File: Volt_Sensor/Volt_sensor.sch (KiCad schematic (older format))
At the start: 23 parts, among them P1 CONN_01X03, P2 CONN_01X02, P3 CONN_01X02, P4 CONN_01X02, U1 LV-25-P, U2 NE5532

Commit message: Changed pot meter
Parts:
- removed RV1: 100k, potentiometer:Potentiometer_Trimmer-Suntan-TSR-3386P, symbol POT-RESCUE-Volt_sensor
- added RV1: 100k, symbol POT
- RV2: symbol POT-RESCUE-Volt_sensor -> POT
- U1: footprint LEM:LV25-P -> Hall-Effect_Transducers_LEM:LV25-P
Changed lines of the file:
@@
 F 0 "U1" H 5800 2200 60  0000 C CNN
 F 1 "LV-25-P" H 6350 1400 60  0000 C CNN
-F 2 "LEM:LV25-P" H 6100 1800 60  0001 C CNN
+F 2 "Hall-Effect_Transducers_LEM:LV25-P" H 6100 1800 60  0001 C CNN
 F 3 "" H 6100 1800 60  0001 C CNN
 	1    6150 1800
@@
 $EndComp
 $Comp
-L POT-RESCUE-Volt_sensor RV1
-U 1 1 583ED8DC
-P 8750 1600
-F 0 "RV1" H 8750 1520 50  0000 C CNN
-F 1 "100k" H 8750 1600 50  0000 C CNN
-F 2 "potentiometer:Potentiometer_Trimmer-Suntan-TSR-3386P" H 8750 1600 50  0001 C CNN
-F 3 "" H 8750 1600 50  0000 C CNN
-	1    8750 1600
-	0    1    1    0
-$EndComp
-$Comp
 L VCC #PWR010
 U 1 1 583ED9DE
@@
 Measurement/\nbypass point
 $Comp
-L POT-RESCUE-Volt_sensor RV2
+L POT RV2
 U 1 1 58501A90
 P 9950 2300
-F 0 "RV2" H 9950 2220 50  0000 C CNN
-F 1 "50k" H 9950 2300 50  0000 C CNN
+F 0 "RV2" V 9850 2300 50  0000 C CNN
+F 1 "50k" V 9950 2300 50  0000 C CNN
 F 2 "potentiometer:Potentiometer_Trimmer-Suntan-TSR-3386P" H 9950 2300 50  0001 C CNN
 F 3 "" H 9950 2300 50  0000 C CNN
 	1    9950 2300
-	-1   0    0    1
+	0    1    1    0
 $EndComp
 Text Notes 9850 2800 0    60   ~ 0
@@
 Text Notes 1200 1850 0    60   ~ 0
 + 15V DC
+$Comp
+L POT RV1
+U 1 1 5980BD14
+P 8750 1600
+F 0 "RV1" V 8650 1600 50  0000 C CNN
+F 1 "100k" V 8750 1600 50  0000 C CNN
+F 2 "" H 8750 1600 50  0001 C CNN
+F 3 "" H 8750 1600 50  0001 C CNN
+	1    8750 1600
+	1    0    0    -1
+$EndComp
 $EndSCHEMATC

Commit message: Updated current sensor card
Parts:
- RV1: footprint (none) -> Potentiometers:Potentiometer_Trimmer_ACP_CA6v_Horizontal
- RV2: footprint potentiometer:Potentiometer_Trimmer-Suntan-TSR-3386P -> Potentiometers:Potentiometer_Trimmer_ACP_CA6v_Horizontal
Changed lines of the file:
@@
 F 0 "RV2" V 9850 2300 50  0000 C CNN
 F 1 "50k" V 9950 2300 50  0000 C CNN
-F 2 "potentiometer:Potentiometer_Trimmer-Suntan-TSR-3386P" H 9950 2300 50  0001 C CNN
+F 2 "Potentiometers:Potentiometer_Trimmer_ACP_CA6v_Horizontal" H 9950 2300 50  0001 C CNN
 F 3 "" H 9950 2300 50  0000 C CNN
 	1    9950 2300
@@
 F 0 "RV1" V 8650 1600 50  0000 C CNN
 F 1 "100k" V 8750 1600 50  0000 C CNN
-F 2 "" H 8750 1600 50  0001 C CNN
+F 2 "Potentiometers:Potentiometer_Trimmer_ACP_CA6v_Horizontal" H 8750 1600 50  0001 C CNN
 F 3 "" H 8750 1600 50  0001 C CNN
 	1    8750 1600

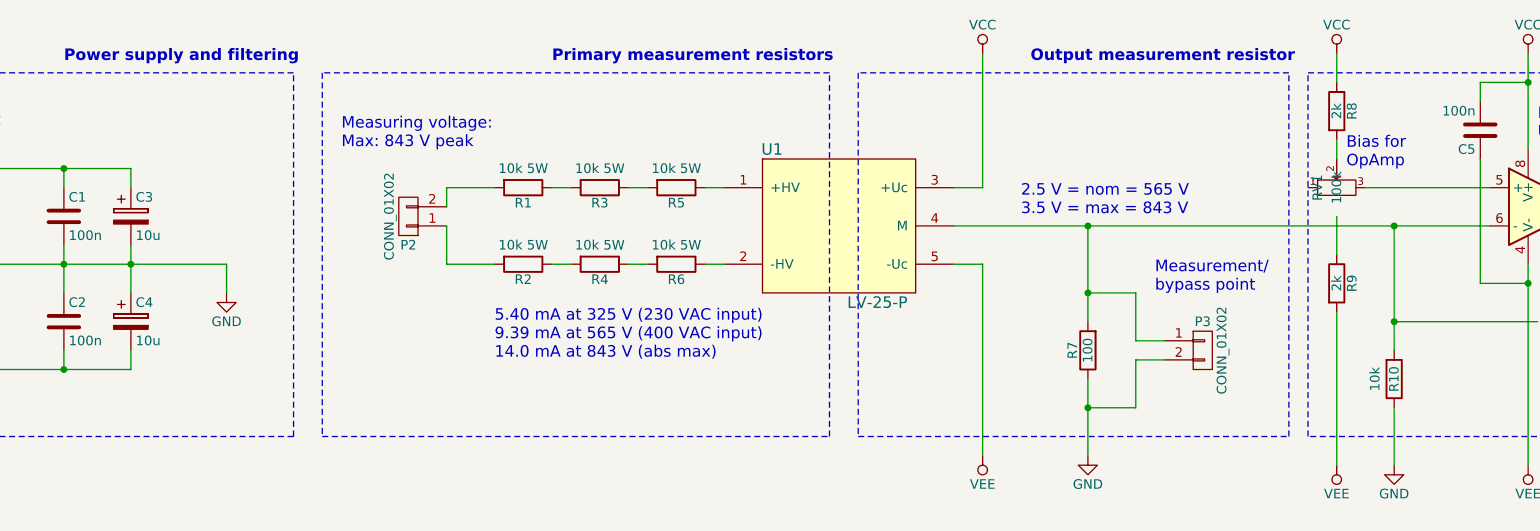
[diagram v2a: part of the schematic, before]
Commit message: Updated component values and highlighted errors and/or improvement possibilities for next revision
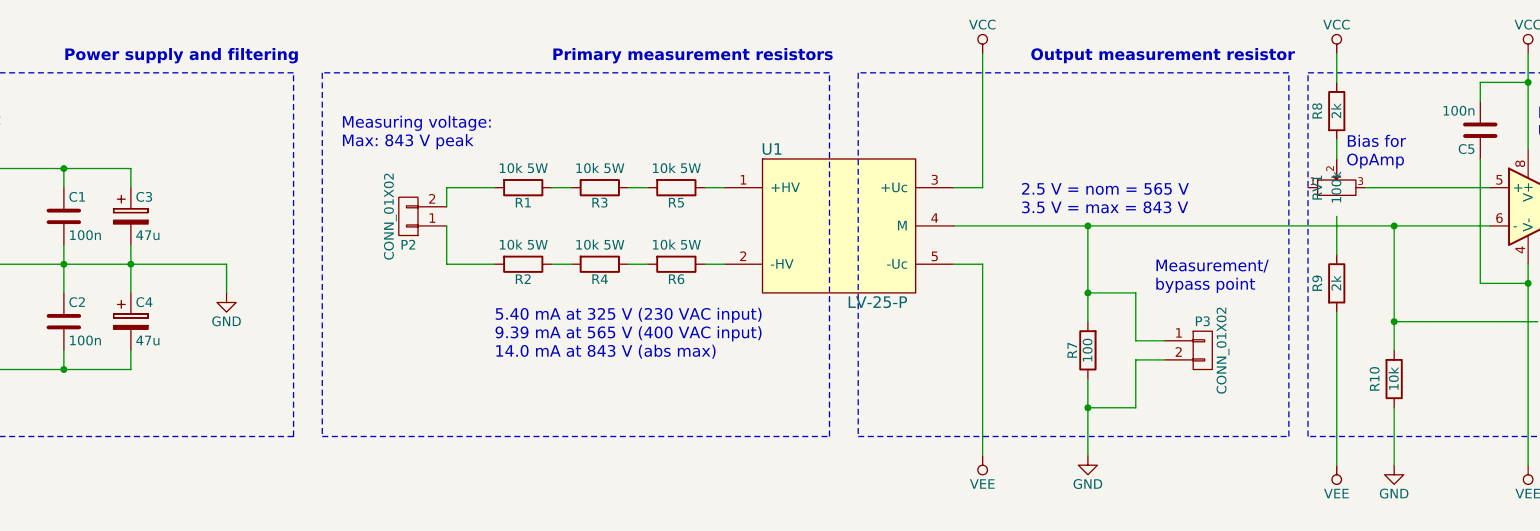
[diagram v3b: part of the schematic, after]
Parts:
- C3, C4: value 10u -> 47u
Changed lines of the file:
@@
 P 2450 2300
 F 0 "C4" H 2475 2400 50  0000 L CNN
-F 1 "10u" H 2475 2200 50  0000 L CNN
+F 1 "47u" H 2475 2200 50  0000 L CNN
 F 2 "Capacitors_THT:C_Radial_D5_L11_P2.5" H 2488 2150 50  0001 C CNN
 F 3 "" H 2450 2300 50  0000 C CNN
@@
 P 2450 1750
 F 0 "C3" H 2475 1850 50  0000 L CNN
-F 1 "10u" H 2475 1650 50  0000 L CNN
+F 1 "47u" H 2475 1650 50  0000 L CNN
 F 2 "Capacitors_THT:C_Radial_D5_L11_P2.5" H 2488 1600 50  0001 C CNN
 F 3 "" H 2450 1750 50  0000 C CNN
@@
 U 1 1 583ED80A
 P 8750 1200
-F 0 "R8" V 8830 1200 50  0000 C CNN
+F 0 "R8" V 8650 1200 50  0000 C CNN
 F 1 "2k" V 8750 1200 50  0000 C CNN
 F 2 "Resistors_SMD:R_1206_HandSoldering" V 8680 1200 50  0001 C CNN
@@
 U 1 1 583ED874
 P 8750 2100
-F 0 "R9" V 8830 2100 50  0000 C CNN
+F 0 "R9" V 8650 2100 50  0000 C CNN
 F 1 "2k" V 8750 2100 50  0000 C CNN
 F 2 "Resistors_SMD:R_1206_HandSoldering" V 8680 2100 50  0001 C CNN
@@
 U 1 1 583EE3A2
 P 9050 2600
-F 0 "R10" V 9050 2600 50  0000 C CNN
-F 1 "10k" V 8950 2600 50  0000 C CNN
+F 0 "R10" V 8950 2600 50  0000 C CNN
+F 1 "10k" V 9050 2600 50  0000 C CNN
 F 2 "Resistors_SMD:R_1206_HandSoldering" V 8980 2600 50  0001 C CNN
 F 3 "" H 9050 2600 50  0000 C CNN

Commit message: Removed some hard-coded paths
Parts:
- C1, C2, C5: symbol C -> device:C
- C3, C4: symbol CP -> device:CP
- P1: symbol CONN_01X03 -> conn:Conn_01x03
- P2, P3, P4: symbol CONN_01X02 -> conn:Conn_01x02
- R1, R10, R2, R3, R4, R5, R6, R7, R8, R9: symbol R -> device:R
- RV1, RV2: symbol POT -> device:POT
- U1: symbol LV-25-P -> LEM:LV-25-P
- U2: symbol NE5532 -> linear:NE5532
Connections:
- wire segments 59 -> 76
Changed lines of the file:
@@
-EESchema Schematic File Version 2
-LIBS:power
-LIBS:device
-LIBS:transistors
-LIBS:conn
-LIBS:linear
-LIBS:regul
-LIBS:74xx
-LIBS:cmos4000
-LIBS:adc-dac
-LIBS:memory
-LIBS:xilinx
-LIBS:microcontrollers
-LIBS:dsp
-LIBS:microchip
-LIBS:analog_switches
-LIBS:motorola
-LIBS:texas
-LIBS:intel
-LIBS:audio
-LIBS:interface
-LIBS:digital-audio
-LIBS:philips
-LIBS:display
-LIBS:cypress
-LIBS:siliconi
-LIBS:opto
-LIBS:atmel
-LIBS:contrib
-LIBS:valves
-LIBS:LEM
-LIBS:Volt_sensor-cache
-EELAYER 25 0
+EESchema Schematic File Version 4
+EELAYER 26 0
 EELAYER END
 $Descr A4 11693 8268
@@
 $EndDescr
 $Comp
-L LV-25-P U1
+L LEM:LV-25-P U1
 U 1 1 583EA5FB
 P 6150 1800
@@
 $EndComp
 $Comp
-L R R1
+L device:R R1
 U 1 1 583EABE7
 P 4500 1600
@@
 $EndComp
 $Comp
-L R R5
+L device:R R5
 U 1 1 583EB13D
 P 5300 1600
@@
 $EndComp
 $Comp
-L R R3
+L device:R R3
 U 1 1 583EB1AE
 P 4900 1600
@@
 $EndComp
 $Comp
-L R R2
+L device:R R2
 U 1 1 583EB1DF
 P 4500 2000
@@
 $EndComp
 $Comp
-L R R6
+L device:R R6
 U 1 1 583EB204
 P 5300 2000
@@
 $EndComp
 $Comp
-L R R4
+L device:R R4
 U 1 1 583EB232
 P 4900 2000
@@
 $EndComp
 $Comp
-L VEE #PWR01
+L power:VEE #PWR01
 U 1 1 583EB25D
 P 6900 3000
@@
 $EndComp
 $Comp
-L VCC #PWR02
+L power:VCC #PWR02
 U 1 1 583EB2AE
 P 6900 900
@@
 $EndComp
 $Comp
-L R R7
+L device:R R7
 U 1 1 583EB372
 P 7450 2450
@@
 $EndComp
 $Comp
-L CONN_01X02 P2
+L conn:Conn_01x02 P2
 U 1 1 583EB545
 P 3900 1750
@@
 $EndComp
 $Comp
-L CONN_01X03 P1
+L conn:Conn_01x03 P1
 U 1 1 583EB6EF
 P 1000 2000
@@
 $EndComp
 $Comp
-L VEE #PWR03
+L power:VEE #PWR03
 U 1 1 583EBA34
 P 1700 2650
@@
 $EndComp
 $Comp
-L VCC #PWR04
+L power:VCC #PWR04
 U 1 1 583EBA60
 P 1700 1400
@@
 $EndComp
 $Comp
-L GND #PWR05
+L power:GND #PWR05
 U 1 1 583EBA8E
 P 7450 3000
@@
 $EndComp
 $Comp
-L GND #PWR06
+L power:GND #PWR06
 U 1 1 583EBAC1
 P 2950 2150
@@
 $EndComp
 $Comp
-L CP C4
+L device:CP C4
 U 1 1 583EBB43
 P 2450 2300
@@
 $EndComp
 $Comp
-L CP C3
+L device:CP C3
 U 1 1 583EBBE1
 P 2450 1750
@@
 $EndComp
 $Comp
-L C C1
+L device:C C1
 U 1 1 583EC499
 P 2100 1750
@@
 $EndComp
 $Comp
-L C C2
+L device:C C2
 U 1 1 583EC55E
 P 2100 2300
@@
 Measuring voltage:\nMax: 843 V peak
 $Comp
-L CONN_01X02 P3
+L conn:Conn_01x02 P3
 U 1 1 583EC98A
 P 8050 2450
@@
 2.5 V = nom = 565 V\n3.5 V = max = 843 V
 $Comp
-L NE5532 U2
+L linear:NE5532 U2
 U 2 1 583ED040
 P 9850 1700
@@
 $EndComp
 $Comp
-L VEE #PWR07
+L power:VEE #PWR07
 U 1 1 583ED138
 P 9750 3050
@@
 $EndComp
 $Comp
-L VCC #PWR08
+L power:VCC #PWR08
 U 1 1 583ED173
 P 9750 900
@@
 $EndComp
 $Comp
-L CONN_01X02 P4
+L conn:Conn_01x02 P4
 U 1 1 583ED366
 P 10750 1750
@@
 $EndComp
 $Comp
-L GND #PWR09
+L power:GND #PWR09
 U 1 1 583ED437
 P 10450 1900
@@
 $EndComp
 $Comp
-L R R8
+L device:R R8
 U 1 1 583ED80A
 P 8750 1200
@@
 $EndComp
 $Comp
-L R R9
+L device:R R9
 U 1 1 583ED874
 P 8750 2100
@@
 $EndComp
 $Comp
-L VCC #PWR010
+L power:VCC #PWR010
 U 1 1 583ED9DE
 P 8750 900
@@
 $EndComp
 $Comp
-L VEE #PWR011
+L power:VEE #PWR011
 U 1 1 583EDA25
 P 8750 3050
@@
 Bias for \nOpAmp
 $Comp
-L R R10
+L device:R R10
 U 1 1 583EE3A2
 P 9050 2600
@@
 $EndComp
 $Comp
-L GND #PWR012
+L power:GND #PWR012
 U 1 1 583EE44C
 P 9050 3050
@@
 $EndComp
 $Comp
-L NE5532 U2
+L linear:NE5532 U2
 U 1 1 583EEB53
 P 1500 5800
@@
 NoConn ~ 1200 5900
 $Comp
-L C C5
+L device:C C5
 U 1 1 583EFAFE
 P 9500 1300
@@
 Measurement/\nbypass point
 $Comp
-L POT RV2
+L device:POT RV2
 U 1 1 58501A90
 P 9950 2300
@@
 	6900 2000 6900 3000
 Wire Wire Line
-	1700 1400 1700 1900
+	1700 1400 1700 1500
 Wire Wire Line
 	1700 1900 1200 1900
 Wire Wire Line
-	1700 2100 1700 2650
+	1700 2100 1700 2550
 Wire Wire Line
 	1200 2100 1700 2100
 Wire Wire Line
-	2450 1900 2450 2150
-Wire Wire Line
-	1200 2000 2950 2000
+	2450 1900 2450 2000
+Wire Wire Line
+	1200 2000 2100 2000
 Connection ~ 2450 2000
 Wire Wire Line
 	2450 1500 2450 1600
 Wire Wire Line
-	1700 1500 2450 1500
+	1700 1500 2100 1500
 Connection ~ 1700 1500
 Wire Wire Line
 	2450 2550 2450 2450
 Wire Wire Line
-	1700 2550 2450 2550
+	1700 2550 2100 2550
 Connection ~ 1700 2550
 Wire Wire Line
@@
 Connection ~ 2100 1500
 Wire Wire Line
-	2100 1900 2100 2150
+	2100 1900 2100 2000
 Wire Wire Line
 	2100 2550 2100 2450
@@
 	8900 1600 9550 1600
 Wire Wire Line
-	6750 1800 9550 1800
-Wire Wire Line
-	10150 1700 10550 1700
+	6750 1800 7450 1800
+Wire Wire Line
+	10150 1700 10250 1700
 Connection ~ 10250 1700
 Wire Wire Line
-	7450 1800 7450 2300
+	7450 1800 7450 2150
 Connection ~ 7450 1800
 Wire Wire Line
-	7450 2600 7450 3000
-Wire Wire Line
-	10100 2300 10250 2300
+	7450 2600 7450 2750
+Wire Wire Line
+	10100 2300 10150 2300
 Wire Wire Line
 	7450 2750 7700 2750
@@
 	8500 1000 6250 1000
 Wire Wire Line
-	9750 2000 9750 3050
+	9750 2000 9750 2100
 Wire Wire Line
 	8750 900  8750 1050
@@
 	10250 2300 10250 1700
 Wire Wire Line
-	9050 1800 9050 2450
+	9050 1800 9050 2300
 Connection ~ 9050 2300
 Connection ~ 9050 1800
@@
 Connection ~ 9750 2100
 Wire Wire Line
-	9750 900  9750 1400
+	9750 900  9750 1050
 Wire Wire Line
 	9500 1150 9500 1050
@@
 + 15V DC
 $Comp
-L POT RV1
+L device:POT RV1
 U 1 1 5980BD14
 P 8750 1600
@@
 	1    0    0    -1
 $EndComp
+Wire Wire Line
+	2450 2000 2450 2150
+Wire Wire Line
+	2450 2000 2950 2000
+Wire Wire Line
+	1700 1500 1700 1900
+Wire Wire Line
+	1700 2550 1700 2650
+Wire Wire Line
+	2100 1500 2450 1500
+Wire Wire Line
+	2100 2550 2450 2550
+Wire Wire Line
+	2100 2000 2450 2000
+Wire Wire Line
+	2100 2000 2100 2150
+Wire Wire Line
+	10250 1700 10550 1700
+Wire Wire Line
+	7450 1800 9050 1800
+Wire Wire Line
+	7450 2750 7450 3000
+Wire Wire Line
+	7450 2150 7450 2300
+Wire Wire Line
+	10150 2300 10250 2300
+Wire Wire Line
+	9050 2300 9050 2450
+Wire Wire Line
+	9050 1800 9550 1800
+Wire Wire Line
+	9750 2100 9750 3050
+Wire Wire Line
+	9750 1050 9750 1400
 $EndSCHEMATC
